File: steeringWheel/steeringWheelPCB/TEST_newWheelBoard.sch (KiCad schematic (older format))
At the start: 38 parts, among them J1 Conn_01x20_Female_OLED, J10 Conn_02x01_Left_Black, J11 Conn_02x01_Blue, J12 Conn_02x01_Green, J13 Conn_02x01_Red, J14 Conn_02x01_Right_Black, J2 Conn_01x09_Female_LED_Right, J3 Conn_01x09_Female_LED_Left, J4 Conn_01x06_Female_Abs_Pos, J5 Conn_02x01_Yellow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

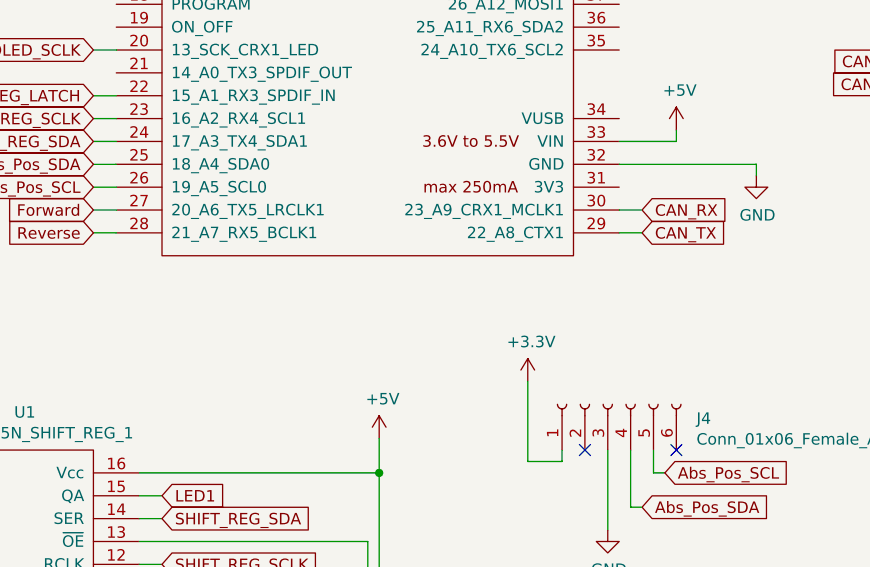
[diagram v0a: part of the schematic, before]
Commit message: Uploading daq KiCad Project
I forgot I generated these files awhile ago (no one from the team bugged me about them, which is a little concerning). Uploading after opening to verify files were complete.
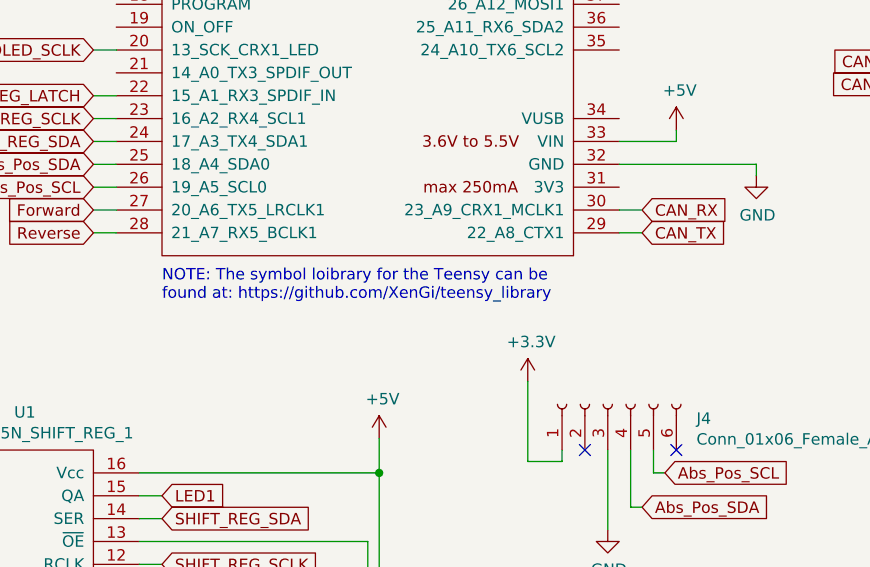
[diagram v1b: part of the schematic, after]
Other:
- note added: "NOTE: The symbol loibrary for the Teensy can be\nfound at: https://github.com/XenGi/teensy_library"
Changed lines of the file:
@@
 EESchema Schematic File Version 4
-LIBS:TEST_newWheelBoard-cache
 EELAYER 30 0
 EELAYER END
@@
 	1    0    0    -1
 $EndComp
+Text Notes 3600 4000 0    50   ~ 0
+NOTE: The symbol loibrary for the Teensy can be\nfound at: https://github.com/XenGi/teensy_library
 $EndSCHEMATC
